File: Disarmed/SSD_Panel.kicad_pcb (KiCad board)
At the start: 2 copper layers, 181.6 x 193 mm, 15 parts, among them J1 Conn_02x04_Counter_Clockwise, U1 MAX7219, U2 MCP41010, U3 MAX7219, U4 MAX7219, U5 MAX7219

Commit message: Footprint update to standard PDIP
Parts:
- U2: footprint Package_DIP:DIP-8-16_W7.62mm -> Package_DIP:DIP-8_W7.62mm
- moved U2 39.4 mm to (99.1, 196.2)
- moved R1 3.18 mm to (115.6, 184.8), turned to 270 degrees
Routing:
- net /SSD_Panel/GND: track 160.2 -> 210.2 mm
- net /SSD_Panel/CLK: track 253.2 -> 203.3 mm, vias 0 -> 1
- net /SSD_Panel/DATA: track 132.3 -> 86.7 mm
- net /SSD_Panel/CCSEL: track 62.0 -> 23.4 mm
- net /SSD_Panel/VCC: track 261.3 -> 232.4 mm
- net /SSD_Panel/ISET: track 183.5 -> 168.7 mm
- net Net-(R1-Pad2): track 23.4 -> 16.2 mm
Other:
- board text added: "Revision 2"
- board text removed: "Revision 1"

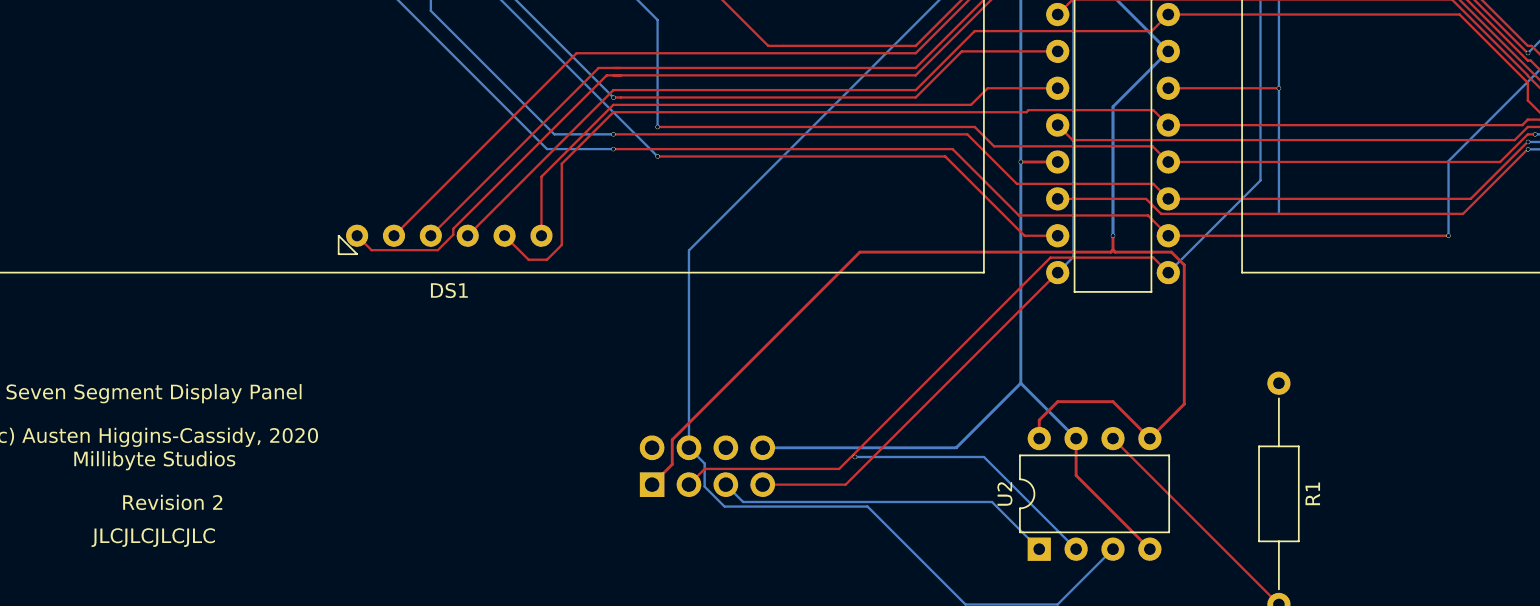
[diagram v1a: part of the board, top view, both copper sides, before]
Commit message: Fix board bug, implement basic driver
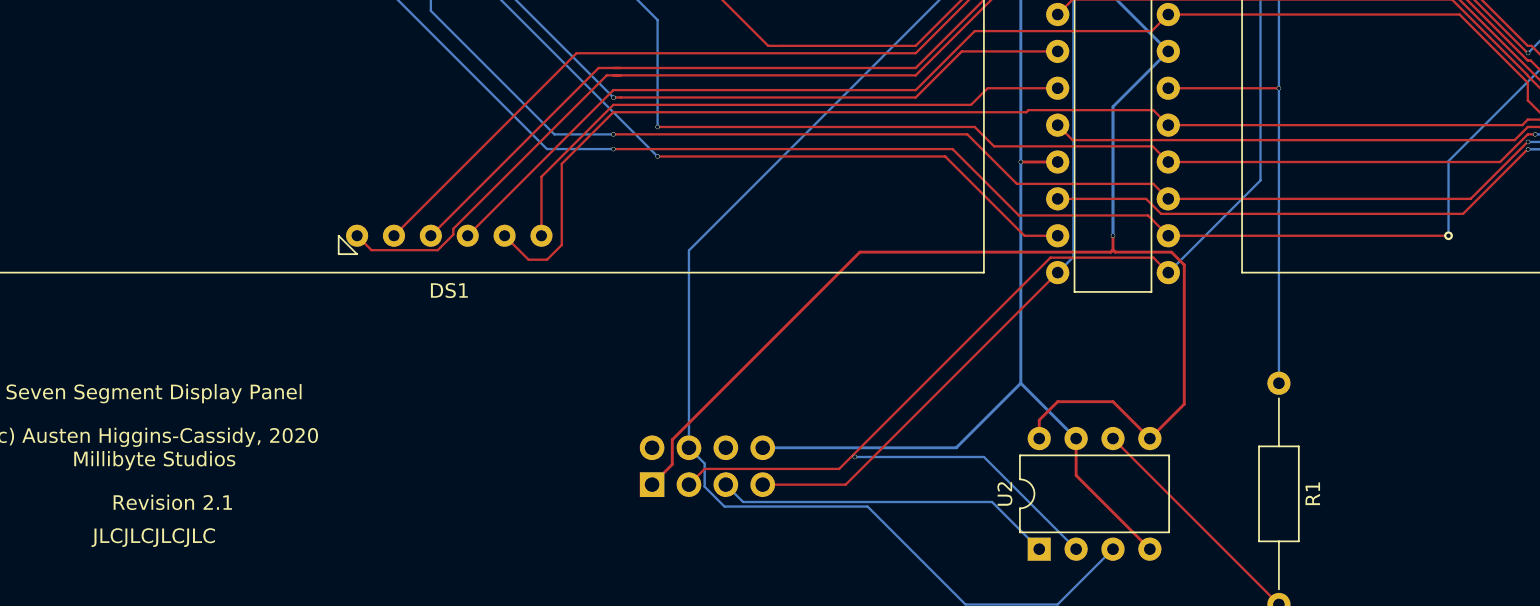
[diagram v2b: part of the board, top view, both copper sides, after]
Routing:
- net /SSD_Panel/ISET: track 168.7 -> 180.5 mm
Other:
- net class Default: via_dia 0.3 -> 0.6; via_drill 0.254 -> 0.3
- net class Power: via_dia 0.3 -> 0.6; via_drill 0.254 -> 0.3
- rule trace_min: 0.1524 -> 0.127
- rule via_min_drill: 0.254 -> 0.3
- rule via_min_size: 0.127 -> 0.6
- board text added: "Revision 2.1"
- board text removed: "Revision 2"

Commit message: Add new boards
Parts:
- removed DS1, DS2, DS3, DS4, DS5, DS6, DS7, DS8: D8014CD, Disarmed:D8041CD
- added C1: 0.1uF, Capacitor_SMD:C_1812_4532Metric_Pad1.57x3.40mm_HandSolder, F.Cu at (57.1, 74.3)
- added C2: 10uF, Capacitor_SMD:C_1812_4532Metric_Pad1.57x3.40mm_HandSolder, F.Cu at (28.2, 67.4)
- added J10: Conn_02x02_Odd_Even, Connector_PinSocket_2.54mm:PinSocket_2x02_P2.54mm_Vertical, F.Cu at (20.3, 50.2)
- added J11: Conn_02x04_Odd_Even, Connector_PinSocket_2.54mm:PinSocket_2x04_P2.54mm_Vertical, F.Cu at (100.3, 22.2)
- added J12: Conn_02x04_Odd_Even, Connector_PinSocket_2.54mm:PinSocket_2x04_P2.54mm_Vertical, F.Cu at (114.3, 61.6)
- added J13: Conn_02x04_Odd_Even, Connector_PinSocket_2.54mm:PinSocket_2x04_P2.54mm_Vertical, F.Cu at (62.2, 22.2)
- added J14: Conn_02x04_Odd_Even, Connector_PinSocket_2.54mm:PinSocket_2x04_P2.54mm_Vertical, F.Cu at (20.3, 34.9)
- added J2: Conn_01x02_Male, Connector_PinHeader_2.54mm:PinHeader_1x02_P2.54mm_Vertical, F.Cu at (48.3, 74.3)
- added J3: Conn_02x02_Odd_Even, Connector_PinSocket_2.54mm:PinSocket_2x02_P2.54mm_Vertical, F.Cu at (74.9, 22.2)
- added J4: Conn_02x02_Odd_Even, Connector_PinSocket_2.54mm:PinSocket_2x02_P2.54mm_Vertical, F.Cu at (114.3, 36.2)
- added J5: Conn_02x02_Odd_Even, Connector_PinSocket_2.54mm:PinSocket_2x02_P2.54mm_Vertical, F.Cu at (36.8, 22.2)
- added J6: Conn_02x02_Odd_Even, Connector_PinSocket_2.54mm:PinSocket_2x02_P2.54mm_Vertical, F.Cu at (20.3, 60.3)
- added J7: Conn_02x02_Odd_Even, Connector_PinSocket_2.54mm:PinSocket_2x02_P2.54mm_Vertical, F.Cu at (85.1, 22.2)
- added J8: Conn_02x02_Odd_Even, Connector_PinSocket_2.54mm:PinSocket_2x02_P2.54mm_Vertical, F.Cu at (114.3, 46.4)
- added J9: Conn_02x02_Odd_Even, Connector_PinSocket_2.54mm:PinSocket_2x02_P2.54mm_Vertical, F.Cu at (47.0, 22.2)
- added R2: RMIN (2K), Resistor_SMD:R_1210_3225Metric_Pad1.30x2.65mm_HandSolder, F.Cu at (86.4, 64.1)
- added R3: RMIN (2K), Resistor_SMD:R_1210_3225Metric_Pad1.30x2.65mm_HandSolder, F.Cu at (66.0, 64.1)
- added R4: RMIN (2K), Resistor_SMD:R_1210_3225Metric_Pad1.30x2.65mm_HandSolder, F.Cu at (106.7, 64.1)
- added R5: 10K, Resistor_SMD:R_1210_3225Metric_Pad1.30x2.65mm_HandSolder, F.Cu at (78.7, 74.3)
- added REF**: MountingHole_4.3mm_M4_Pad_Via, Disarmed:MountingHole_4.3mm_M4_Pad_Via, F.Cu at (113.0, 23.5)
- added REF**: MountingHole_4.3mm_M4_Pad_Via, Disarmed:MountingHole_4.3mm_M4_Pad_Via, F.Cu at (113.0, 75.6)
- added REF**: MountingHole_4.3mm_M4_Pad_Via, Disarmed:MountingHole_4.3mm_M4_Pad_Via, F.Cu at (21.6, 75.6)
- added REF**: MountingHole_4.3mm_M4_Pad_Via, Disarmed:MountingHole_4.3mm_M4_Pad_Via, F.Cu at (21.6, 23.5)
- added RV1: R_POT, 3362P-1-103LF:TRIM_3362P-1-103LF, F.Cu at (36.8, 64.1)
- added RV2: R_POT, 3362P-1-103LF:TRIM_3362P-1-103LF, F.Cu at (77.5, 64.1)
- added RV3: R_POT, 3362P-1-103LF:TRIM_3362P-1-103LF, F.Cu at (57.1, 64.1)
- added RV4: R_POT, 3362P-1-103LF:TRIM_3362P-1-103LF, F.Cu at (97.8, 64.1)
- J1: value Conn_02x04_Counter_Clockwise -> Conn_02x03_Odd_Even; footprint Connector_PinSocket_2.54mm:PinSocket_2x04_P2.54mm_Vertical -> Connector_PinHeader_2.54mm:PinHeader_2x03_P2.54mm_Vertical; moved to F.Cu
- R1: value 2k -> RMIN (2K); footprint Resistor_THT:R_Axial_DIN0207_L6.3mm_D2.5mm_P15.24mm_Horizontal -> Resistor_SMD:R_1210_3225Metric_Pad1.30x2.65mm_HandSolder
- U1: value MAX7219 -> ATTINY85-20PU; footprint Package_DIP:DIP-24_W7.62mm -> digikey-footprints:DIP-8_W7.62mm
- U2: value MCP41010 -> MAX7219; footprint Package_DIP:DIP-8_W7.62mm -> Package_DIP:DIP-24_W7.62mm
- moved U2 180.2 mm to (33.0, 28.6), turned to 0 degrees
- moved R1 139.4 mm to (45.7, 64.1), turned to 0 degrees
- moved J1 124.0 mm to (36.8, 73.0)
- moved U3 90.6 mm to (53.3, 28.6)
- moved U1 79.5 mm to (64.8, 78.1), turned to 90 degrees
- moved U4 43.4 mm to (73.7, 28.6)
- moved U5 10.9 mm to (94.0, 28.6)
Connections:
- J1 pad 1: /SSD_Panel/VCC -> /MISO_DATA
- J1 pad 2: Net-(J1-Pad2) -> +5V
- J1 pad 3: /SSD_Panel/CLK -> /SCK_SCL
- J1 pad 4: /SSD_Panel/DATA -> /MOSI_SDA
- J1 pad 5: /SSD_Panel/CCSEL -> /RST
- J1 pad 6: Net-(J1-Pad6) -> GND
- R1 pad 1: /SSD_Panel/ISET -> Net-(R1-Pad1)
- R1 pad 2: Net-(R1-Pad2) -> +5V
- U1 pad 1: /SSD_Panel/DATA -> /RST
- U1 pad 2: /SSD_Panel/DIG0 -> /CLK
- U1 pad 3: /SSD_Panel/DIG4 -> /LOAD
- U1 pad 4: /SSD_Panel/GND -> GND
- U1 pad 5: /SSD_Panel/DIG6 -> /MOSI_SDA
- U1 pad 6: /SSD_Panel/DIG2 -> /MISO_DATA
- U1 pad 7: /SSD_Panel/DIG3 -> /SCK_SCL
- U1 pad 8: /SSD_Panel/DIG7 -> +5V
- U2 pad 1: /SSD_Panel/CCSEL -> /MISO_DATA
- U2 pad 2: /SSD_Panel/CLK -> /DIG0
- U2 pad 3: /SSD_Panel/DATA -> /DIG4
- U2 pad 4: /SSD_Panel/GND -> GND
- U2 pad 5: /SSD_Panel/VCC -> /DIG6
- U2 pad 6: Net-(R1-Pad2) -> /DIG2
- U2 pad 7: /SSD_Panel/GND -> /DIG3
- U2 pad 8: /SSD_Panel/VCC -> /DIG7
- U3 pad 1: Net-(U1-Pad24) -> Net-(U2-Pad24)
- U3 pad 10: /SSD_Panel/DIG13 -> /DIG13
- U3 pad 11: /SSD_Panel/DIG9 -> /DIG9
- U3 pad 12: /SSD_Panel/LOAD -> /LOAD
- U3 pad 13: /SSD_Panel/CLK -> /CLK
- U3 pad 14: /SSD_Panel/A2 -> /A2
- U3 pad 15: /SSD_Panel/F2 -> /F2
- U3 pad 16: /SSD_Panel/B2 -> /B2
- U3 pad 17: /SSD_Panel/G2 -> /G2
- U3 pad 18: /SSD_Panel/ISET -> /ISET2
- U3 pad 19: /SSD_Panel/VCC -> +5V
- U3 pad 2: /SSD_Panel/DIG8 -> /DIG8
- U3 pad 20: /SSD_Panel/C2 -> /C2
- U3 pad 21: /SSD_Panel/E2 -> /E2
- U3 pad 22: /SSD_Panel/DP2 -> /DP2
- U3 pad 23: /SSD_Panel/D2 -> /D2
- U3 pad 3: /SSD_Panel/DIG12 -> /DIG12
- U3 pad 4: /SSD_Panel/GND -> GND
- U3 pad 5: /SSD_Panel/DIG14 -> /DIG14
- U3 pad 6: /SSD_Panel/DIG10 -> /DIG10
- U3 pad 7: /SSD_Panel/DIG11 -> /DIG11
- U3 pad 8: /SSD_Panel/DIG15 -> /DIG15
- U3 pad 9: /SSD_Panel/GND -> GND
- U4 pad 10: /SSD_Panel/DIG21 -> /DIG21
- U4 pad 11: /SSD_Panel/DIG17 -> /DIG17
- U4 pad 12: /SSD_Panel/LOAD -> /LOAD
- U4 pad 13: /SSD_Panel/CLK -> /CLK
- U4 pad 14: /SSD_Panel/A3 -> /A3
- U4 pad 15: /SSD_Panel/F3 -> /F3
- U4 pad 16: /SSD_Panel/B3 -> /B3
- U4 pad 17: /SSD_Panel/G3 -> /G3
- U4 pad 18: /SSD_Panel/ISET -> /ISET3
- U4 pad 19: /SSD_Panel/VCC -> +5V
- U4 pad 2: /SSD_Panel/DIG16 -> /DIG16
- U4 pad 20: /SSD_Panel/C3 -> /C3
- U4 pad 21: /SSD_Panel/E3 -> /E3
- U4 pad 22: /SSD_Panel/DP3 -> /DP3
- U4 pad 23: /SSD_Panel/D3 -> /D3
- U4 pad 3: /SSD_Panel/DIG20 -> /DIG20
- U4 pad 4: /SSD_Panel/GND -> GND
- U4 pad 5: /SSD_Panel/DIG22 -> /DIG22
- U4 pad 6: /SSD_Panel/DIG18 -> /DIG18
- U4 pad 7: /SSD_Panel/DIG19 -> /DIG19
- U4 pad 8: /SSD_Panel/DIG23 -> /DIG23
- U4 pad 9: /SSD_Panel/GND -> GND
- U5 pad 10: /SSD_Panel/DIG29 -> /DIG29
- U5 pad 11: /SSD_Panel/DIG25 -> /DIG25
- U5 pad 12: /SSD_Panel/LOAD -> /LOAD
- U5 pad 13: /SSD_Panel/CLK -> /CLK
- U5 pad 14: /SSD_Panel/A4 -> /A4
- U5 pad 15: /SSD_Panel/F4 -> /F4
- U5 pad 16: /SSD_Panel/B4 -> /B4
- U5 pad 17: /SSD_Panel/G4 -> /G4
- U5 pad 18: /SSD_Panel/ISET -> /ISET4
- U5 pad 19: /SSD_Panel/VCC -> +5V
- U5 pad 2: /SSD_Panel/DIG24 -> /DIG24
- U5 pad 20: /SSD_Panel/C4 -> /C4
- U5 pad 21: /SSD_Panel/E4 -> /E4
- U5 pad 22: /SSD_Panel/DP4 -> /DP4
- U5 pad 23: /SSD_Panel/D4 -> /D4
- U5 pad 24: Net-(U5-Pad24) -> (no net)
- U5 pad 3: /SSD_Panel/DIG28 -> /DIG28
- U5 pad 4: /SSD_Panel/GND -> GND
- U5 pad 5: /SSD_Panel/DIG30 -> /DIG30
- U5 pad 6: /SSD_Panel/DIG26 -> /DIG26
- U5 pad 7: /SSD_Panel/DIG27 -> /DIG27
- U5 pad 8: /SSD_Panel/DIG31 -> /DIG31
- U5 pad 9: /SSD_Panel/GND -> GND
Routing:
- net GND: track 0.00 -> 262.8 mm, vias 0 -> 12
- net +5V: track 0.00 -> 245.5 mm, vias 0 -> 3
- net /SSD_Panel/VCC: track 232.4 -> 0.00 mm, vias 6 -> 0
- net /SSD_Panel/GND: track 210.2 -> 0.00 mm, vias 8 -> 0
- net /SSD_Panel/CLK: track 203.3 -> 0.00 mm, vias 1 -> 0
- net /SSD_Panel/ISET: track 180.5 -> 0.00 mm, vias 4 -> 0
- net /SSD_Panel/LOAD: track 158.6 -> 0.00 mm
- net /LOAD: track 0.00 -> 141.9 mm
- net /SSD_Panel/A1: track 117.1 -> 0.00 mm, vias 2 -> 0
- net /SSD_Panel/A4: track 117.1 -> 0.00 mm, vias 2 -> 0
- net /SSD_Panel/A3: track 117.1 -> 0.00 mm, vias 2 -> 0
- net /SSD_Panel/A2: track 117.1 -> 0.00 mm, vias 2 -> 0
- net /SSD_Panel/F1: track 114.4 -> 0.00 mm, vias 2 -> 0
- net /SSD_Panel/F4: track 114.4 -> 0.00 mm, vias 2 -> 0
- net /SSD_Panel/F3: track 114.4 -> 0.00 mm, vias 2 -> 0
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- added copper zone on B.Cu, net GND
- added copper zone on F.Cu, net GND
- removed copper zone on B.Cu, net /SSD_Panel/GND
- removed copper zone on F.Cu, net /SSD_Panel/GND
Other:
- board size 181.6 x 193 mm -> 104.1 x 64.8 mm
- net class Default: clearance 0.1524 -> 0.15; trace_width 0.16 -> 0.2
- net class Power: clearance 0.2 -> 0.15; trace_width 0.2 -> 0.4
- rule trace_clearance: 0.1524 -> 0.15
- board text added: "Revision 5"
- board text added: "SSD Control Panel (c) Austen Higgins-Cassidy Millibyte Studios"
- board text removed: "(c) Austen Higgins-Cassidy, 2020 Millibyte Studios"
- board text removed: "Revision 2.1"
- board text removed: "Seven Segment Display Panel"
